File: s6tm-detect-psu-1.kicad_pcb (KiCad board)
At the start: 4 copper layers, 50 x 50 mm, 120 parts, among them J1 Conn_01x02, J2 Conn_01x02, J3 USB_C_Receptacle_USB2.0_14P, J4 Conn_01x04, J5 Conn_01x04, J6 Conn_01x04_Pin, J7 TC2030, SW1 SW_Push, SW2 SW_Push, U1 TPS259470x, U2 TPS259470x, U3 TPS259470x, U4 TPS62933, U5 TPS259470x, U6 SN65HVD230, U7 HT753-1, U8 STM32F103C8Tx, Y1 8M

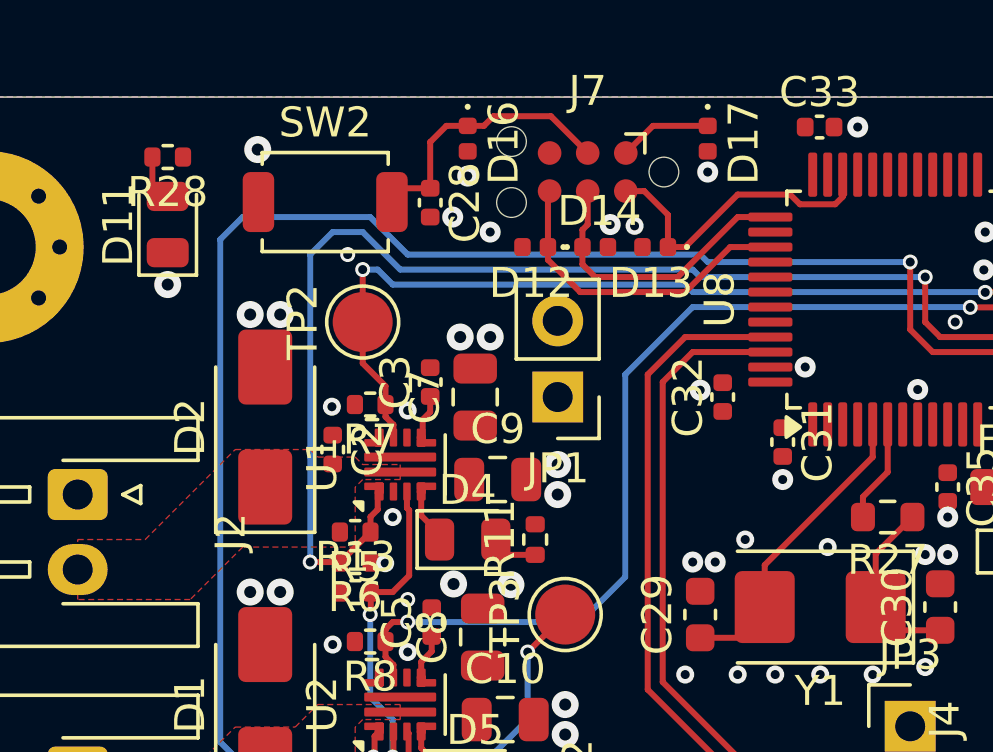
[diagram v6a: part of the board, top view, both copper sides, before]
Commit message: pcb: add can led routing
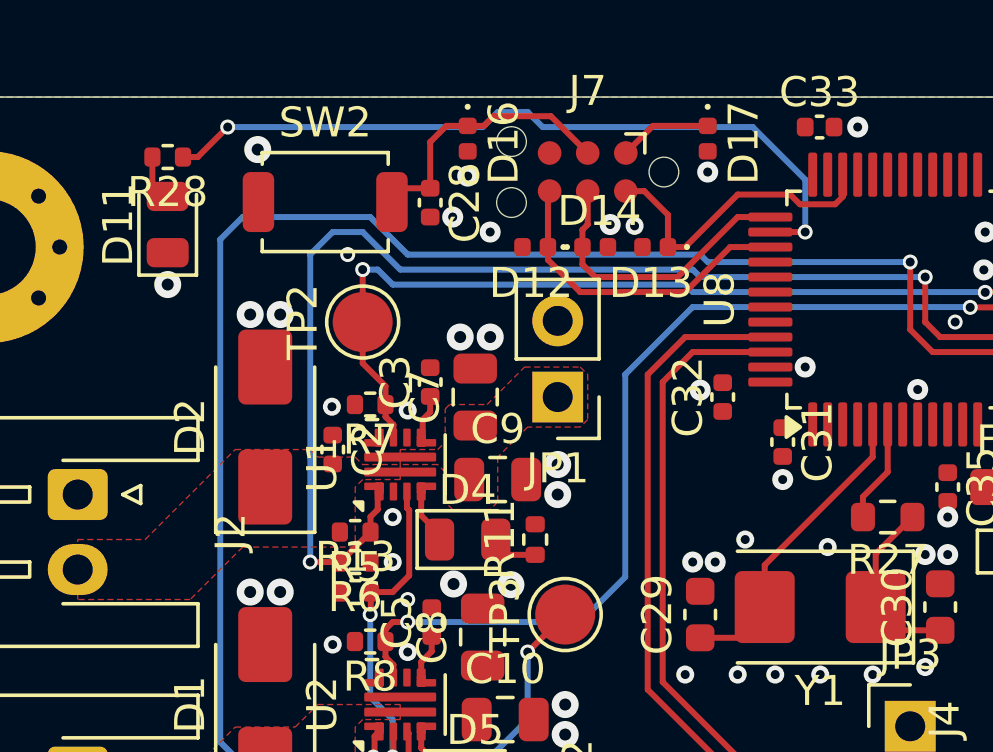
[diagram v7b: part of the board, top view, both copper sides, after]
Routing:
- net Net-(U8-PA15): track 0.00 -> 25.2 mm, vias 0 -> 2
- added copper zone on F.Cu, net +BATT
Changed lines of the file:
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@@
 	)
 	(via
-		(at 117.25 121.538885)
+		(at 117.5 121.5)
 		(size 0.6)
 		(drill 0.3)
@@
 	)
 	(segment
+		(start 111 108)
+		(end 110.51 108)
+		(width 0.2)
+		(layer "F.Cu")
+		(net "Net-(U8-PA15)")
+	)
+	(segment
+		(start 112 107)
+		(end 111 108)
+		(width 0.2)
+		(layer "F.Cu")
+		(net "Net-(U8-PA15)")
+	)
+	(segment
+		(start 131.25 110.5)
+		(end 130.0875 110.5)
+		(width 0.2)
+		(layer "F.Cu")
+		(net "Net-(U8-PA15)")
+	)
+	(via
+		(at 131.25 110.5)
+		(size 0.5)
+		(drill 0.3)
+		(layers "F.Cu" "B.Cu")
+		(net "Net-(U8-PA15)")
+	)
+	(via
+		(at 112 107)
+		(size 0.5)
+		(drill 0.3)
+		(layers "F.Cu" "B.Cu")
+		(net "Net-(U8-PA15)")
+	)
+	(segment
+		(start 121 106.5)
+		(end 122 106.5)
+		(width 0.2)
+		(layer "B.Cu")
+		(net "Net-(U8-PA15)")
+	)
+	(segment
+		(start 131.25 108.75)
+		(end 131.25 110.5)
+		(width 0.2)
+		(layer "B.Cu")
+		(net "Net-(U8-PA15)")
+	)
+	(segment
+		(start 120.5 107)
+		(end 121 106.5)
+		(width 0.2)
+		(layer "B.Cu")
+		(net "Net-(U8-PA15)")
+	)
+	(segment
+		(start 129.5 107)
+		(end 131.25 108.75)
+		(width 0.2)
+		(layer "B.Cu")
+		(net "Net-(U8-PA15)")
+	)
+	(segment
+		(start 122 106.5)
+		(end 122.5 107)
+		(width 0.2)
+		(layer "B.Cu")
+		(net "Net-(U8-PA15)")
+	)
+	(segment
+		(start 122.5 107)
+		(end 129.5 107)
+		(width 0.2)
+		(layer "B.Cu")
+		(net "Net-(U8-PA15)")
+	)
+	(segment
+		(start 112 107)
+		(end 120.5 107)
+		(width 0.2)
+		(layer "B.Cu")
+		(net "Net-(U8-PA15)")
+	)
+	(segment
 		(start 123.75 112.5)
 		(end 122.675 111.425)
@@
 	)
 	(zone
+		(net "+BATT")
+		(layer "F.Cu")
+		(hatch edge 0.5)
+		(priority 5)
+		(connect_pads yes
+			(clearance 0.2)
+		)
+		(min_thickness 0.15)
+		(fill yes
+			(thermal_gap 0.5)
+			(thermal_bridge_width 0.5)
+			(island_removal_mode 0)
+		)
+		(polygon
+			(pts
+				(xy 117.75 117.75) (xy 119 117.75) (xy 119.25 117.5) (xy 119.25 116.396448) (xy 119.396448 116.25)
+				(xy 120.646448 116.25) (xy 121.896448 115) (xy 123.75 115) (xy 124 115.25) (xy 124 116.75) (xy 123.75 117)
+				(xy 122 117) (xy 121 118) (xy 121 119.5) (xy 120.75 119.75) (xy 119.5 119.75) (xy 119.25 119.5)
+				(xy 119.25 118.5) (xy 119 118.25) (xy 117.75 118.25)
+			)
+		)
+	)
+	(zone

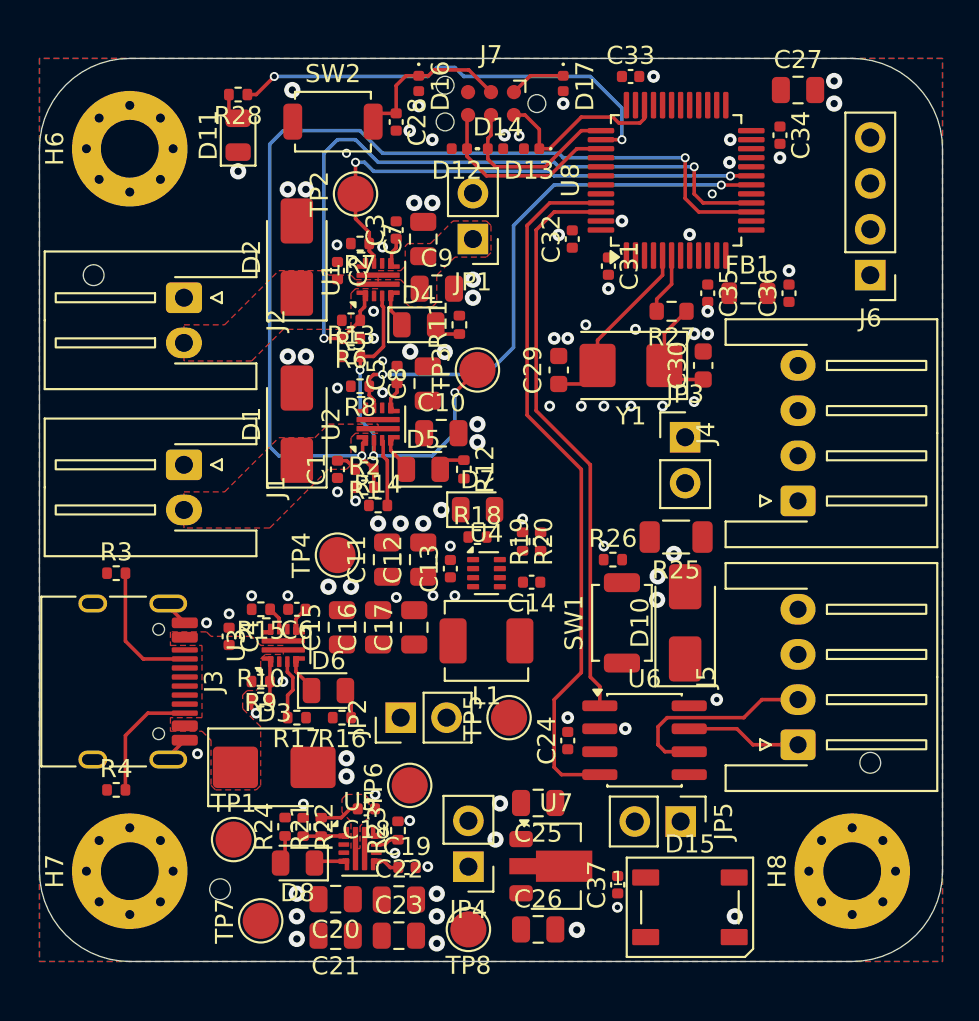
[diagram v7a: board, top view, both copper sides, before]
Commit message: pcb: route efuse signals
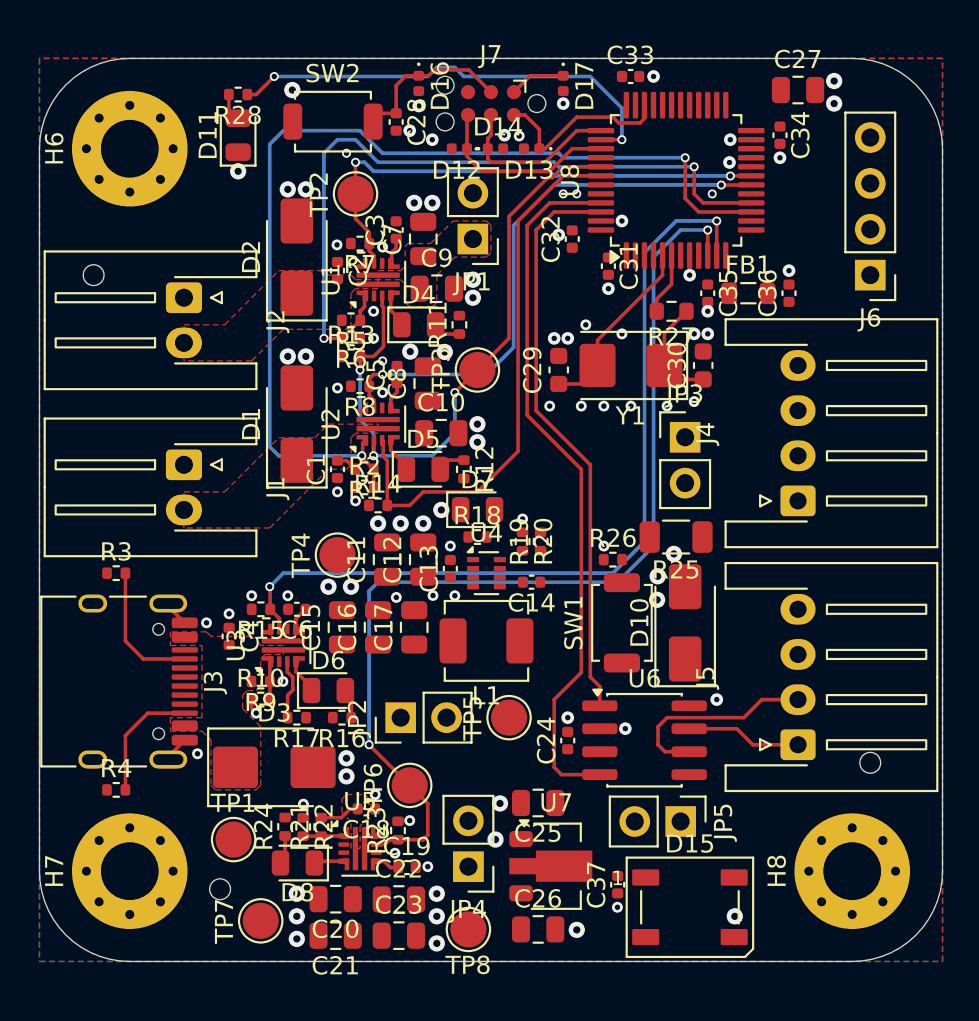
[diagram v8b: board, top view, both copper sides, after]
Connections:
- U8 pad 29: IN1 -> unconnected-(U8-PA8-Pad29)
- U8 pad 30: IN2 -> unconnected-(U8-PA9-Pad30)
- U8 pad 31: IN2 -> unconnected-(U8-PA10-Pad31)
- U8 pad 41: unconnected-(U8-PB5-Pad41) -> IN1
- U8 pad 42: unconnected-(U8-PB6-Pad42) -> IN2
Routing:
- net ILM4: track 1.31 -> 55.7 mm, vias 0 -> 2
- net ILM3: track 1.31 -> 47.0 mm, vias 0 -> 2
- net IN2: track 3.72 -> 30.6 mm
- net IN1: track 20.1 -> 35.5 mm
- net GND: vias 98 -> 100
